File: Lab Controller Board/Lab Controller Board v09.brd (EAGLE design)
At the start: 50 x 50 mm, 49 parts, among them Q2 MMBT5088, Q3 100A/100V, Q4 MMBT5088, Q5 100A/100V, Q6 MMBT5088, Q7 100A/100V, Q8 MMBT5088, U1 ATMEGA328P_TQFP, U2 CH340G, U3 +12v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

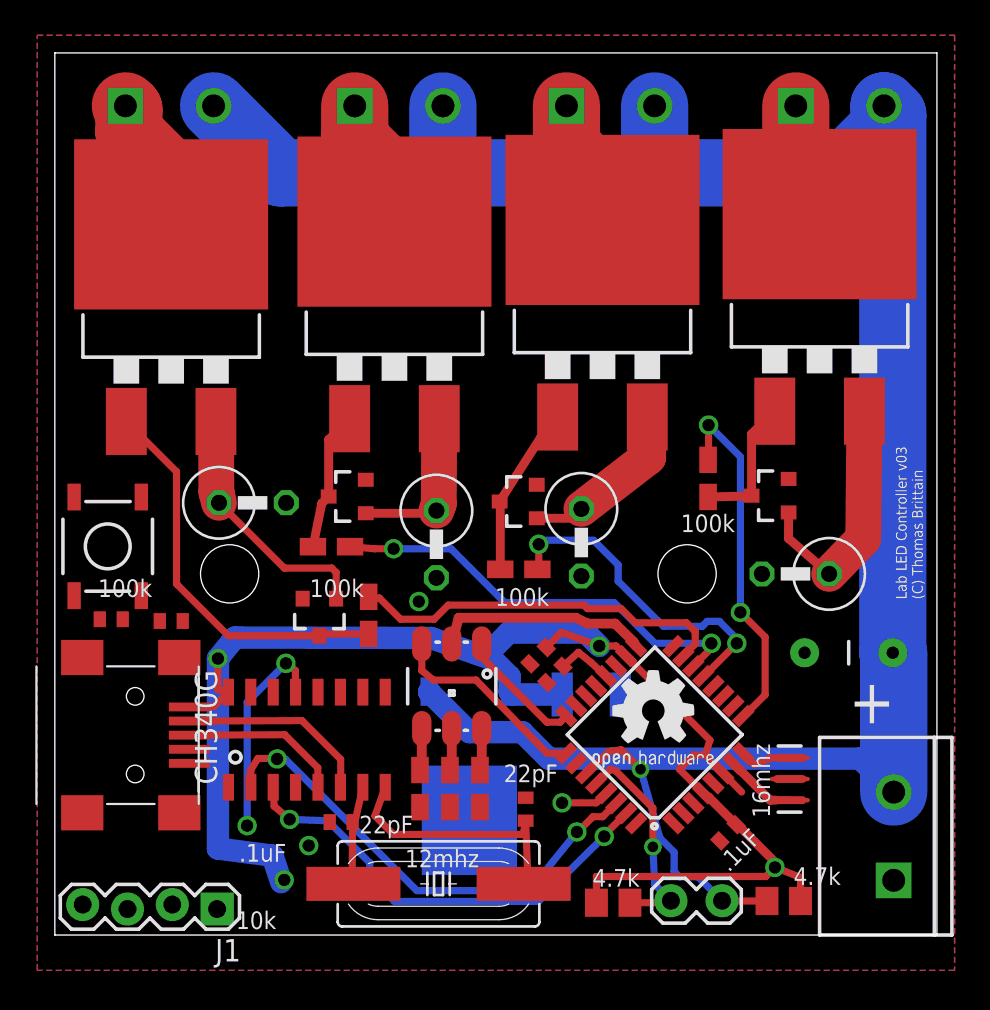
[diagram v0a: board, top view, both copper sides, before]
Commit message: Added ESP-07, RX/TX level converter, temp probe connection.  Cleaned silkscreen
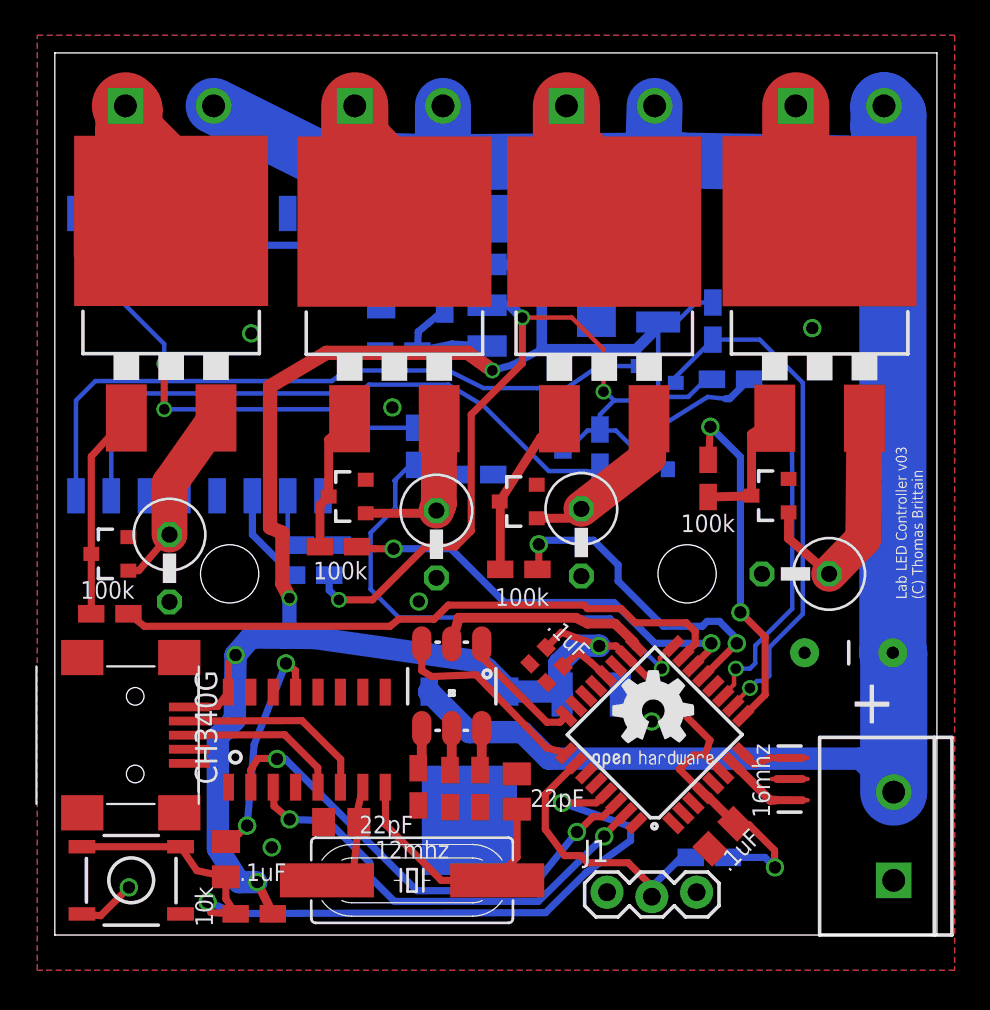
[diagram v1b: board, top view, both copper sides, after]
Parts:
- removed JP8: (no value), SparkFun-Connectors:1X02_LOCK
- added C10: 10uF, SparkFun-Capacitors:EIA3528
- added C11: 470uF, resistor:D/7343-31W
- added C9: 0.1uF, resistor:C0805K
- added Q9: MOSFET-NCHANNELAO3404A, SparkFun-DiscreteSemi:SOT23-3
- added R15, R19, R20, R21, R22: 10k, resistor:R0805W
- added R16: 3.3k, resistor:R0805W
- added R17: 220, resistor:R0805W
- added R18: 370, resistor:R0805W
- added R23: 20k, resistor:R0805W
- added RESONATOR: 16mhz, crystal:HC49UP
- added U$1: ESP8266-07, lio:ESP-07
- added U4: V_REG_317SMD, SparkFun-PowerIC:SOT223
- C4, C5, C6, C7: device resistor:C0402 -> resistor:C0805K
- CN1: value (none) -> USB_CON
- J1: value (none) -> DS18B20; device SparkFun-Connectors:1X04_LOCK -> SparkFun-Connectors:1X03_LOCK
- JP1: value (none) -> 12V_INPUT
- JP2: value (none) -> LED_THREE
- JP3: value (none) -> LED_TWO
- JP4: value (none) -> LED_ONE
- JP5: value (none) -> LED_FOUR
- Q1: value (none) -> MOSFET-NCHANNELAO3404A; device crystal:HC49UP -> SparkFun-DiscreteSemi:SOT23-3
- R10: value 4.7k -> 3.3k; device resistor:M0805 -> resistor:R0805W
- R14: device resistor:R0402 -> resistor:R0805W
- R9: value 4.7k -> 10k; device resistor:M0805 -> resistor:R0805W
- moved GOLD_ORB_SM1 47.0 mm to (5.57, 1.08), turned to 90 degrees
- moved Q1 31.0 mm to (34.1, 31.3), flipped to the bottom, turned to 90 degrees
- moved R10 25.3 mm to (14.5, 20.4), flipped to the bottom, turned to 0 degrees
- moved J1 22.1 mm to (31.3, 2.30), turned to 0 degrees
- moved S1 19.0 mm to (4.33, 3.10), turned to 180 degrees
- moved R14 17.3 mm to (11.3, 1.20)
- moved C5 15.1 mm to (9.70, 4.30), turned to 270 degrees
- moved R3 14.7 mm to (3.12, 18.2), turned to 180 degrees
- moved Q4 12.3 mm to (3.17, 21.6), turned to 90 degrees
- moved R4 6.89 mm to (6.50, 20.2), turned to 270 degrees
- moved R9 4.89 mm to (37.1, 4.40), flipped to the bottom, turned to 180 degrees
- moved C7 1.12 mm to (26.2, 8.13)
- moved R1 0.40 mm to (16.1, 22.0)
- moved Q5 0.40 mm to (43.4, 36.3)
- moved C4 0.36 mm to (37.9, 5.60)
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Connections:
- removed net 2: J1.3, U1.32
- removed net 3: J1.2, U1.1
- removed net 4: U1.2
- removed net 6: U1.10
- removed net 7: U1.11
- removed net 8: U1.12
- removed net A0: U1.23
- removed net A6: U1.19
- removed net A7: U1.22
- removed net ID: CN1.ID
- removed net N$32: U2.4
- removed net SCL: JP8.1, R10.1, U1.28
- removed net SDA: JP8.2, R9.1, U1.27
- new net 3.35V: C11.+, C9.1, Q1.1, Q9.1, R10.1, R17.2, R21.2, R22.2, U$1.CH_PD, U$1.VCC, U4.2
- new net ESP-RX: Q9.3, R19.1, U1.11
- new net ESP-TX: Q1.3, R20.1, U1.10
- new net N$12: Q1.2, R22.1, U$1.TXD
- new net N$14: R17.1, R18.2, U4.1
- new net N$15: Q9.2, R21.1, U$1.RXD
- new net N$3: R15.1, U$1.REST
- new net N$4: R10.2, U$1.GPIO2
- new net N$5: R16.2, U$1.GPIO15
- net 12: now also R15.2, R23.2
- net A3: now also J1.2, R9.1
- net GND: now also C10.C, C11.-, C9.2, J1.3, R16.1, R18.1, R23.1, U$1.GND
- net VCC: now also C10.A, R19.2, R20.2, U4.3; no longer J1.4, R10.2
- net X0: now also RESONATOR.2; no longer Q1.2
- net X1: now also RESONATOR.1; no longer Q1.1
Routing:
- net 3.35V: track 0.00 -> 73.2 mm, vias 0 -> 3
- net N$13: track 2.82 -> 46.6 mm, vias 1 -> 2
- net VCC: track 89.9 -> 130.9 mm, vias 4 -> 6
- net N$12: track 0.00 -> 39.8 mm
- net N$15: track 0.00 -> 37.3 mm
- net 12: track 0.00 -> 30.9 mm, vias 0 -> 1
- net ESP-TX: track 0.00 -> 29.6 mm, vias 0 -> 1
- net ESP-RX: track 0.00 -> 28.3 mm, vias 0 -> 1
- net N$3: track 0.00 -> 27.8 mm, vias 0 -> 2
- net A3: track 0.00 -> 17.7 mm
- net SDA: track 16.3 -> 0.00 mm, vias 1 -> 0
- net 11: track 21.7 -> 35.1 mm
- net SCL: track 12.4 -> 0.00 mm, vias 1 -> 0
- net PWM_B1: track 23.5 -> 13.0 mm
- net N$14: track 0.00 -> 7.04 mm
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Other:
- board text added: "1uF"
- board text added: "20k"
- board text added: "220"
- board text added: "370"
- board text added: "470uF"
- board text added: "BSS138"
- board text added: "ESP8266-07"
- board text added: "Lab LED Controller v09 (C) Thomas Brittain"
- board text removed: "4.7k"
- board text removed: "Lab LED Controller v05 (C) Thomas Brittain"
